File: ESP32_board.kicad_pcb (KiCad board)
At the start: 4 copper layers, 90.9 x 54.6 mm, 86 parts, among them J1 SS-52400-002, J2 B2B-PH-SM4-TB, J3 GSD090012SEU, J4 Conn_01x04_Pin, J5 Conn_01x05_Pin, Q1 TEMT6000X01, Q2 BC817, Q3 BC817, U1 MCP73871, U2 BME280, U3 ESP32-C3-WROOM-02-H4, U4 CP2102N-Axx-xQFN20, U5 USBLC6-2SC6, U6 W25Q32JVSSIQ, U7 MAX4466EXK

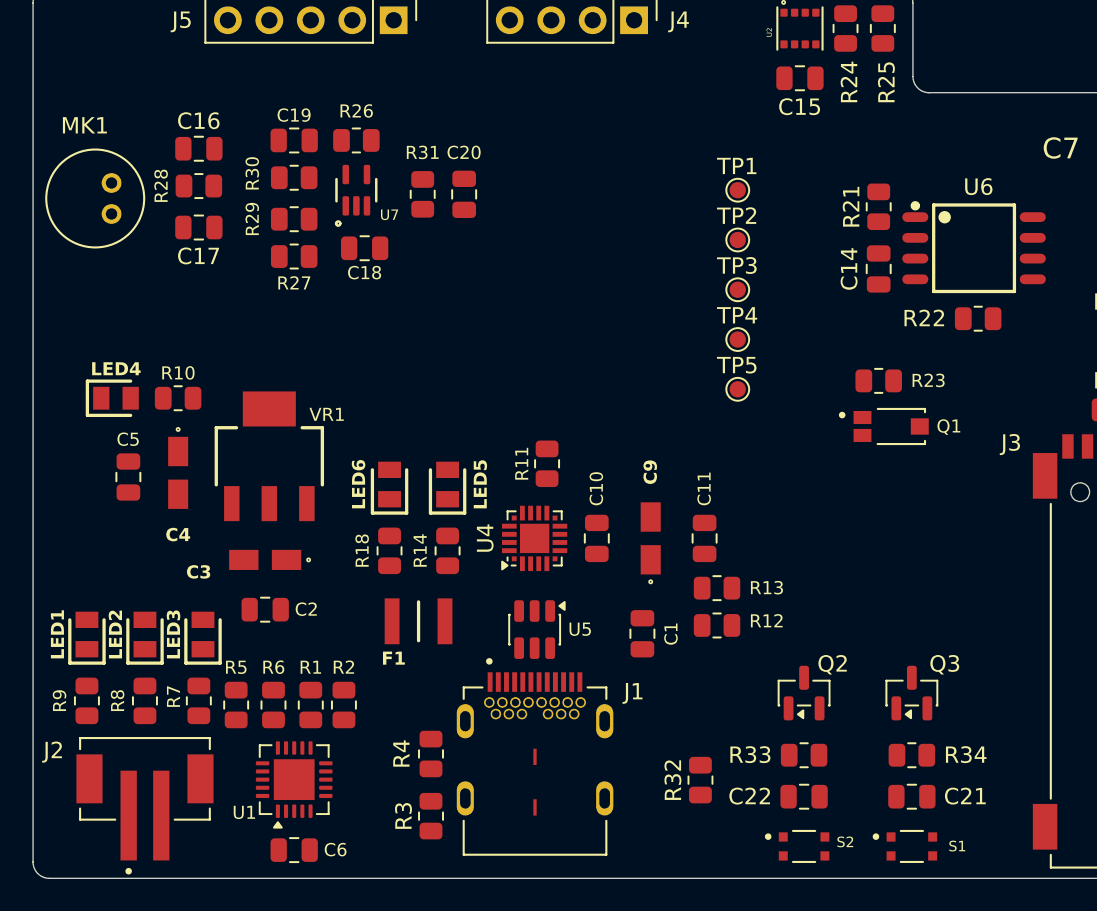
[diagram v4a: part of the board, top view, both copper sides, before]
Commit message: finished copper pours
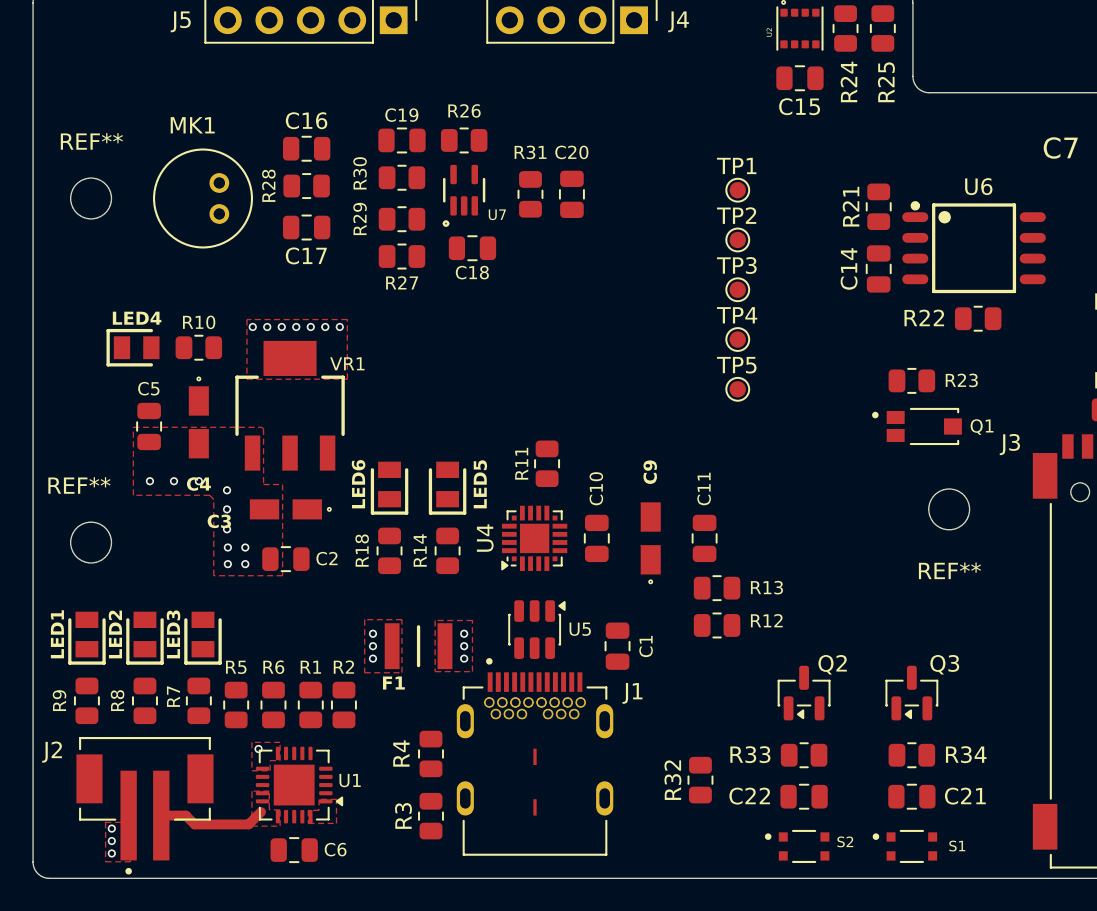
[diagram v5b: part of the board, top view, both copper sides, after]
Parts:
- added REF**: MountingHole_2.5mm, MountingHole:MountingHole_2.5mm, F.Cu at (167.9, 115.1)
- added REF**: MountingHole_2.5mm, MountingHole:MountingHole_2.5mm, F.Cu at (167.9, 94.0)
- added REF**: MountingHole_2.5mm, MountingHole:MountingHole_2.5mm, F.Cu at (220.5, 113.0)
- moved C16 6.60 mm to (181.1, 90.9)
- moved C17 6.60 mm to (181.1, 95.8)
- moved C18 6.60 mm to (191.3, 97.0)
- moved C20 6.60 mm to (197.4, 93.7)
- moved MK1 6.60 mm to (174.8, 94.0)
- moved R28 6.60 mm to (181.1, 93.2)
- moved R31 6.60 mm to (194.8, 93.7)
- moved C19 6.60 mm to (186.9, 90.4)
- moved R26 6.60 mm to (190.8, 90.4)
- moved R27 6.60 mm to (186.9, 97.5)
- moved R29 6.60 mm to (186.9, 95.2)
- moved R30 6.60 mm to (186.9, 92.7)
- moved U7 6.60 mm to (190.8, 93.5)
- moved C2 3.35 mm to (179.8, 116.1)
- moved C3 3.35 mm to (179.8, 113.0)
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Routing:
- net /VBAT: track 0.00 -> 6.65 mm
- net GND: vias 0 -> 14
- net /VBUS: vias 0 -> 3
- net /+5V_USB: vias 0 -> 3
- net +3V3: vias 0 -> 7
- added copper zone on F.Cu, net +3V3
- added copper zone on In1.Cu, net +3V3
- added copper zone on F.Cu, net +5V
- added copper zone on F.Cu, net /+5V_USB
- added copper zone on In1.Cu, net /+5V_USB
- added copper zone on F.Cu, net /VBAT
- added copper zone on F.Cu, net /VBUS
- added copper zone on In1.Cu, net /VBUS
- added copper zone on F.Cu, net GND
- added copper zone on In2.Cu, net GND

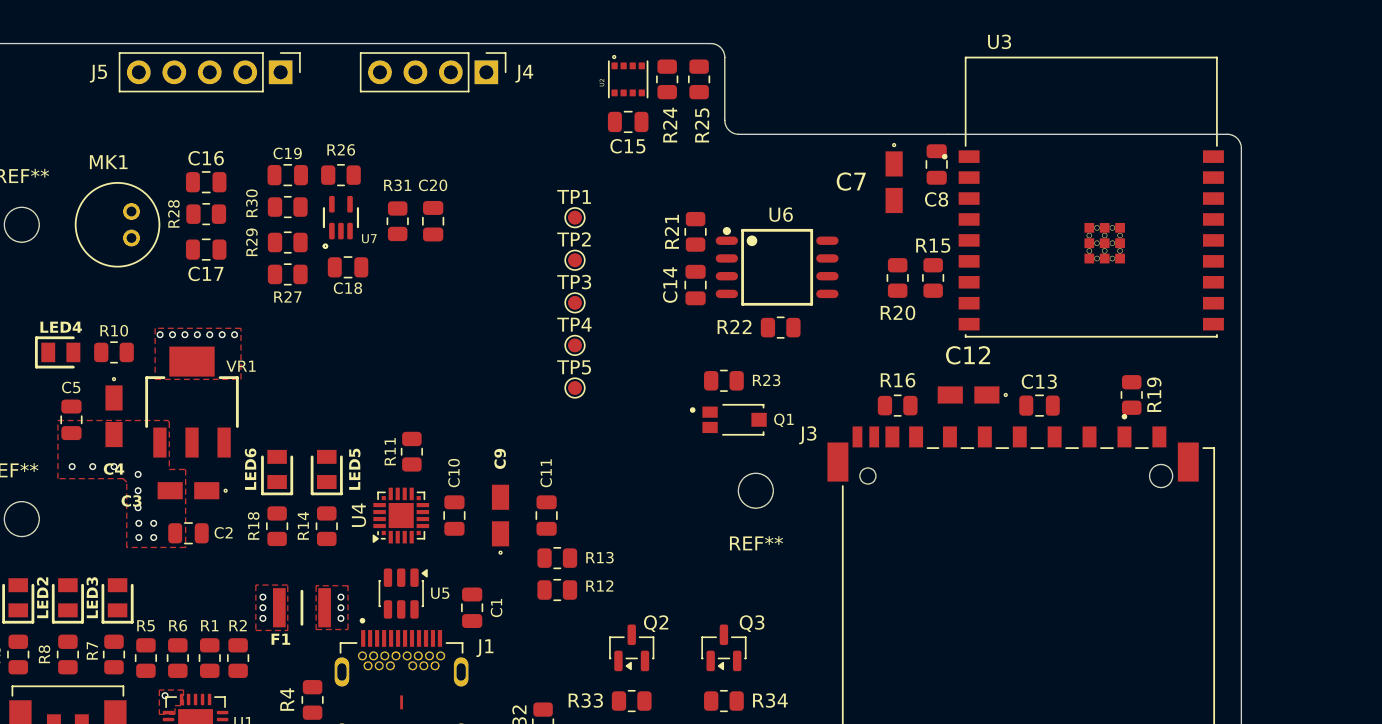
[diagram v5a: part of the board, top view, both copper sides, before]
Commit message: finished I2C routing
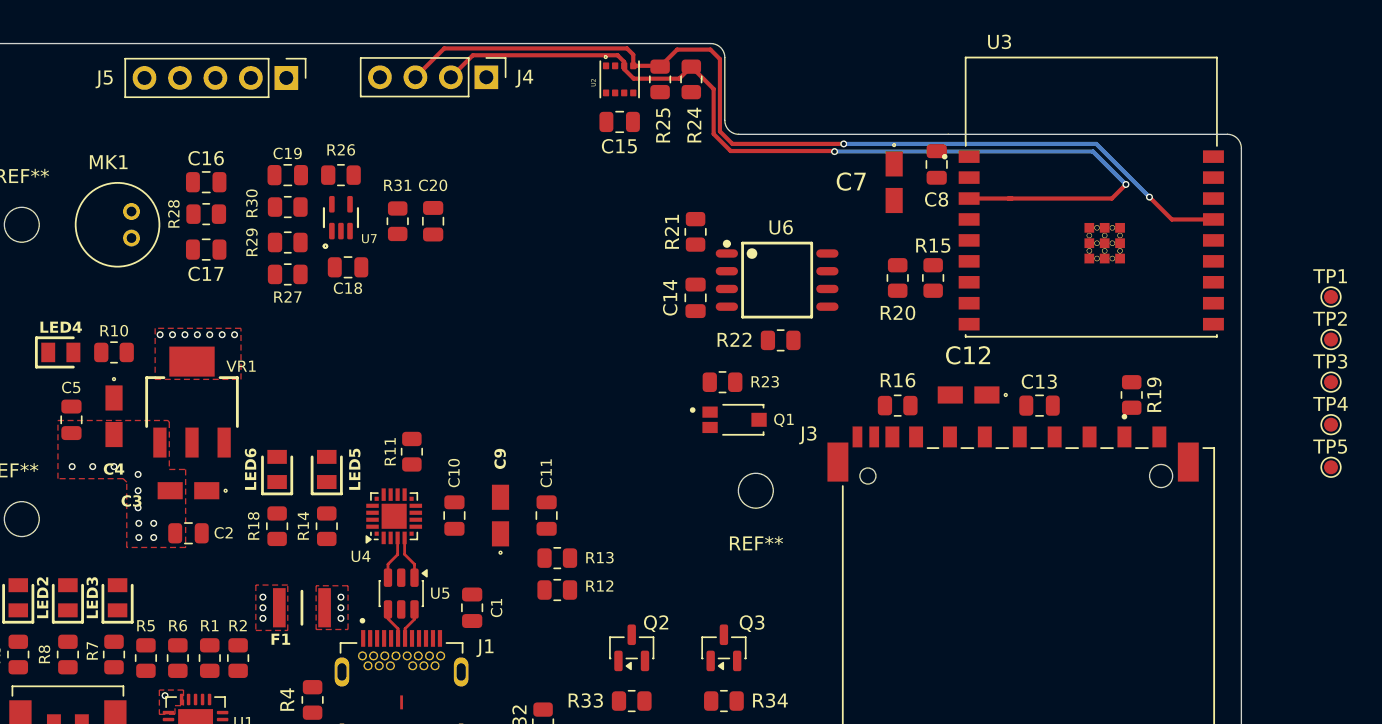
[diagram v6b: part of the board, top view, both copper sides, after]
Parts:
- moved TP1 54.4 mm to (261.7, 99.2)
- moved TP2 54.4 mm to (261.7, 102.2)
- moved TP3 54.4 mm to (261.7, 105.2)
- moved TP4 54.4 mm to (261.7, 108.3)
- moved TP5 54.4 mm to (261.7, 111.3)
- moved R25 2.79 mm to (213.6, 83.6)
- moved R24 1.73 mm to (215.8, 83.6)
- moved C14 0.91 mm to (216.2, 99.2)
- moved R22 0.91 mm to (222.2, 102.3)
- moved U6 0.91 mm to (222.0, 97.9)
- moved C15 0.61 mm to (210.7, 86.6)
- moved U2 0.61 mm to (210.7, 83.6)
- moved J5 0.57 mm to (186.8, 83.5)
- moved U4 0.51 mm to (194.6, 114.9)
- moved J4 0.36 mm to (201.2, 83.4)
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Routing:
- net /ESP32-C3-02/SCL: track 0.00 -> 67.6 mm, vias 0 -> 2
- net /ESP32-C3-02/SDA: track 0.00 -> 67.4 mm, vias 0 -> 2
- net /ESP32-C3-02/USB_D-: track 0.00 -> 3.14 mm
- net /ESP32-C3-02/USB_D+: track 0.00 -> 3.14 mm
- net /USB_DP: track 0.00 -> 2.38 mm
- net /USB_DN: track 0.00 -> 2.36 mm

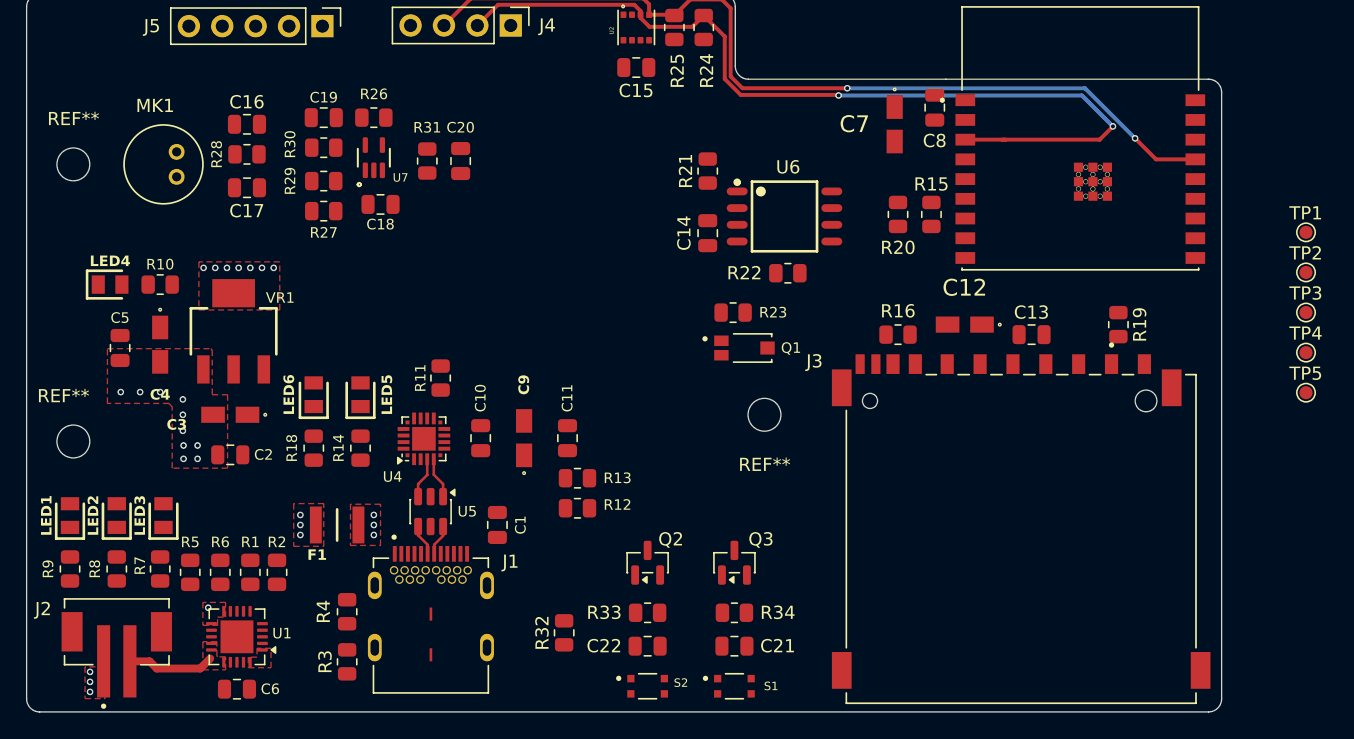
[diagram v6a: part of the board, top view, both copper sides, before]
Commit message: finished routing SPI signals
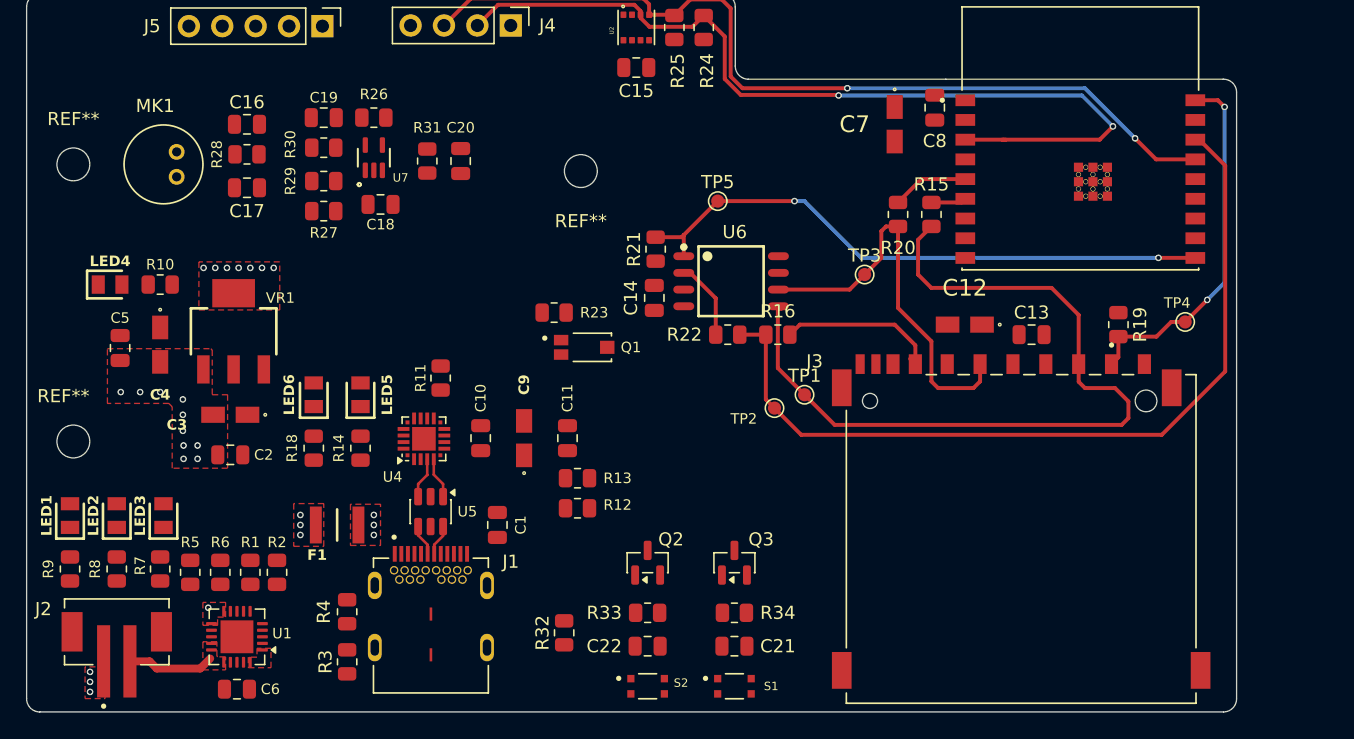
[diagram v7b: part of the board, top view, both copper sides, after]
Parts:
- moved TP5 47.1 mm to (216.9, 96.8)
- moved TP2 41.7 mm to (221.2, 112.5)
- moved TP1 40.1 mm to (223.5, 111.5)
- moved TP3 33.7 mm to (228.1, 102.4)
- moved REF** 23.2 mm to (206.5, 94.5)
- moved R23 13.6 mm to (204.5, 105.3)
- moved Q1 12.2 mm to (206.8, 107.9)
- moved TP4 9.49 mm to (252.5, 106.0)
- moved R16 9.14 mm to (221.5, 106.9)
- moved R21 7.14 mm to (212.2, 100.4)
- moved R22 6.54 mm to (217.7, 106.9)
- moved U6 6.39 mm to (217.9, 102.9)
- moved C14 6.39 mm to (212.1, 104.1)
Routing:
- net /ESP32-C3-02/MISO_DO: track 0.00 -> 63.7 mm
- net /ESP32-C3-02/MOSI_DI: track 0.00 -> 62.0 mm
- net /ESP32-C3-02/CS~: track 0.00 -> 45.6 mm, vias 0 -> 2
- net /ESP32-C3-02/SCLK: track 0.00 -> 30.6 mm
- net /ESP32-C3-02/CS_SD: track 0.00 -> 27.9 mm, vias 0 -> 2
- net /ESP32-C3-02/MISO_DO_SD: track 0.00 -> 12.5 mm
- net /ESP32-C3-02/MISO_DO_FLASH: track 0.00 -> 6.00 mm
- net /ESP32-C3-02/SCLK_ESP32: track 0.00 -> 5.85 mm
- net /ESP32-C3-02/MOSI_DI_ESP32: track 0.00 -> 2.69 mm
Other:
- board size 90.9 x 54.6 mm -> 92 x 54.6 mm

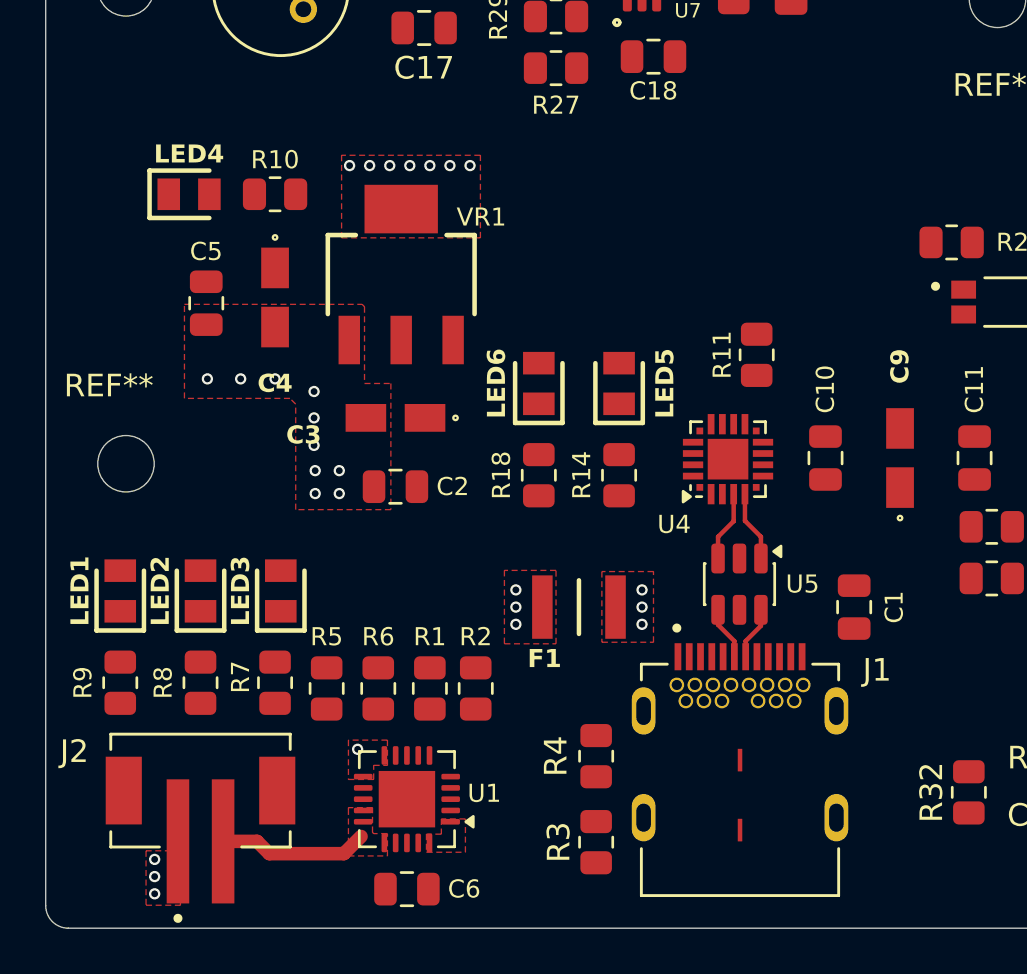
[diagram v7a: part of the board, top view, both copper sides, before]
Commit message: almost finished routing power traces
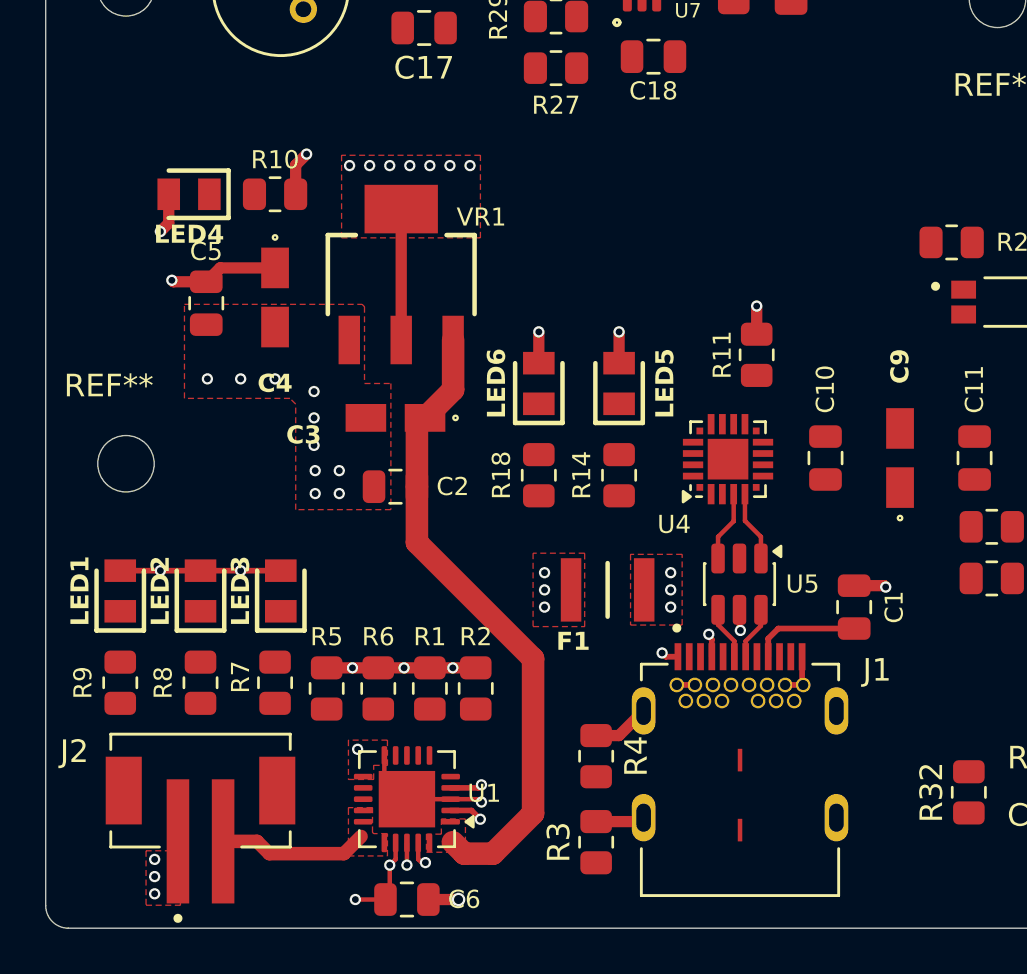
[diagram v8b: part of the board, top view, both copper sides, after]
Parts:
- moved F1 1.48 mm to (189.2, 120.7)
- moved C6 0.46 mm to (180.3, 134.4)
- turned LED4 to 180 degrees
- turned R4 to 90 degrees
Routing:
- net +5V: track 0.00 -> 28.3 mm
- net GND: track 0.00 -> 25.4 mm, vias 14 -> 22
- net +3V3: track 0.00 -> 16.5 mm, vias 7 -> 12
- net /+5V_USB: track 0.00 -> 16.3 mm, vias 3 -> 11
- net /VBUS: track 0.00 -> 6.80 mm, vias 3 -> 5
